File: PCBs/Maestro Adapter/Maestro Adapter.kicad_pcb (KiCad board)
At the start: 2 copper layers, 15 parts

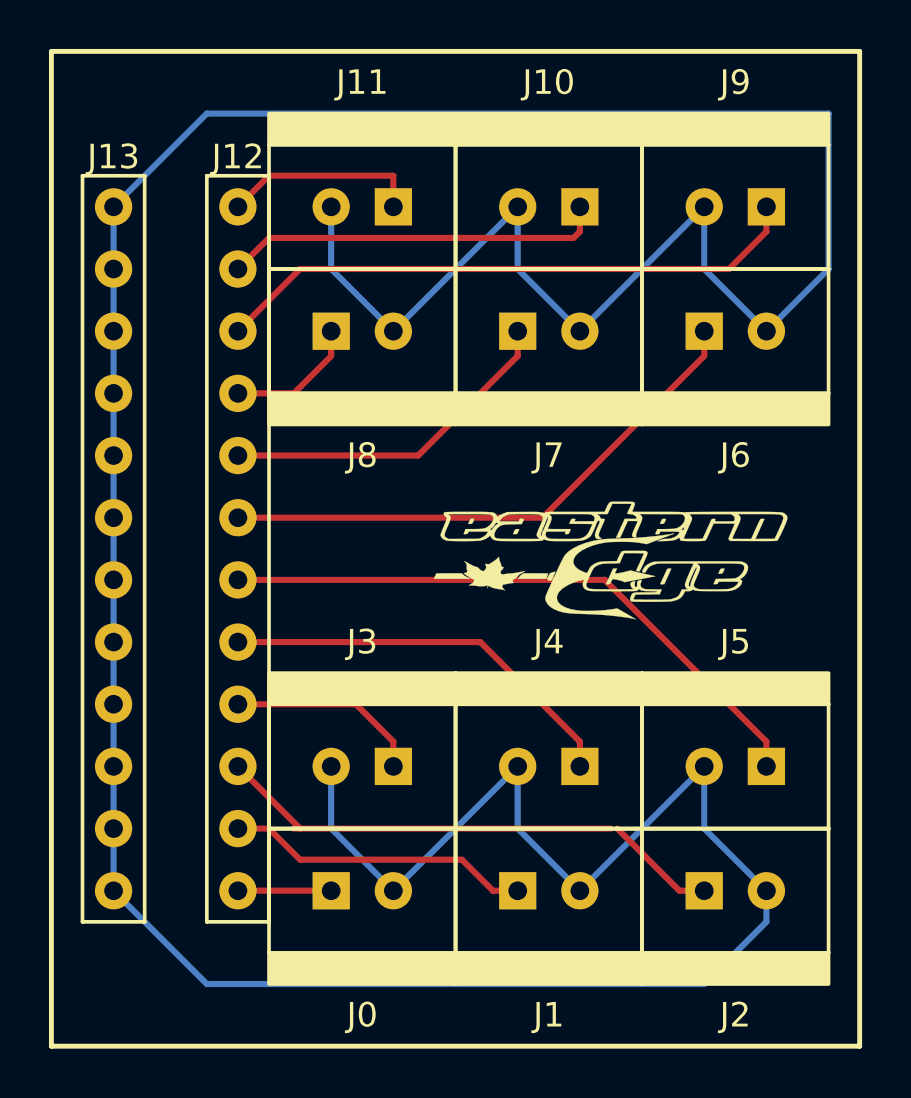
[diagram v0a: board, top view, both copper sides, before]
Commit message: added spot for missed gap in servo channels
missed a gap between channel 5 and 6. so added additional pads
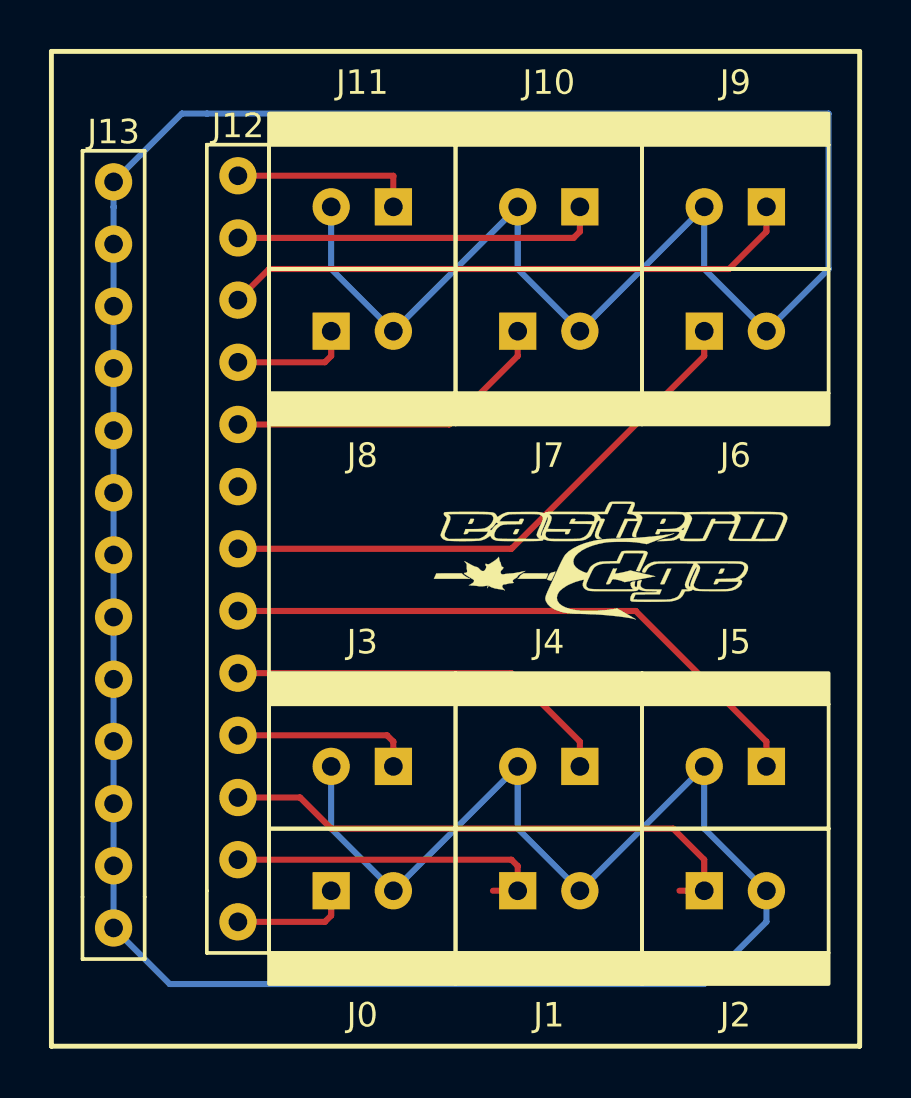
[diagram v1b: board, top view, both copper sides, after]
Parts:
- J12, J13: footprint through hole:1x12 through hole -> through hole:1x13 through hole
- moved J12 1.27 mm to (78.7, 88.9)
- moved J13 1.02 mm to (73.7, 89.2)
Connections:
- J12 pad 11: Net-(J1-Pad1) -> Net-(J12-Pad11)
- J12 pad 12: Net-(J0-Pad1) -> Net-(J1-Pad1)
- J2 pad 1: Net-(J12-Pad10) -> Net-(J12-Pad11)
- J3 pad 1: Net-(J12-Pad9) -> Net-(J12-Pad10)
- J4 pad 1: Net-(J12-Pad8) -> Net-(J12-Pad9)
- J5 pad 1: Net-(J12-Pad7) -> Net-(J12-Pad8)
- J6 pad 1: Net-(J12-Pad6) -> Net-(J12-Pad7)
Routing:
- net Net-(J12-Pad6): track 22.8 -> 0.00 mm
- net Net-(J12-Pad11): track 0.00 -> 22.4 mm
- net Net-(J12-Pad10): track 21.2 -> 7.47 mm
- net Net-(J12-Pad8): track 16.7 -> 24.8 mm
- net Net-(J12-Pad9): track 7.99 -> 16.1 mm
- net Net-(J12-Pad7): track 25.3 -> 23.3 mm
- net GND: track 164.8 -> 166.3 mm
- net Net-(J0-Pad1): track 3.81 -> 4.93 mm
- net Net-(J1-Pad1): track 12.5 -> 13.6 mm
- net Net-(J12-Pad5): track 14.1 -> 13.6 mm
- net Net-(J12-Pad3): track 24.3 -> 23.8 mm
- net Net-(J12-Pad4): track 5.45 -> 4.93 mm
- net Net-(J11-Pad1): track 8.15 -> 7.62 mm
- net Net-(J10-Pad1): track 15.6 -> 15.1 mm

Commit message: Added Colour to 3D Model
We probably have to change the footprint again anyways, but at least now its in colour!!!
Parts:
- J0, J1, J10, J11, J2, J3, J4, J5, J6, J7, J8, J9: value (none) -> Conn_01x02_Female; footprint through hole:1x2_molex_llc -> EER:1x2_molex_llc
- J12, J13: value (none) -> Conn_01x13_Male

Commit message: Completed List of suggestions
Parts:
- removed the ? at (94.0, 106.7)
- removed J0, J1, J10, J11, J2, J3, J4, J5, J6, J7, J8, J9: Conn_01x02_Female, EER:1x2_molex_llc
- added ?: , MountingHole:MountingHole_3.2mm_M3_Pad, F.Cu at (157.5, 64.8)
- added ?: , MountingHole:MountingHole_3.2mm_M3_Pad, F.Cu at (101.6, 64.8)
- added ?: , MountingHole:MountingHole_3.2mm_M3_Pad, F.Cu at (101.6, 124.5)
- added ?: , MountingHole:MountingHole_3.2mm_M3_Pad, F.Cu at (157.5, 124.5)
- added ?: , EER:EERLOGO, F.Cu at (127.0, 74.9)
- added Channel 0: , EER:1x2_molex_llc, F.Cu at (149.9, 120.7)
- added Channel 1: , EER:1x2_molex_llc, F.Cu at (149.9, 111.8)
- added Channel 10: , EER:1x2_molex_llc, F.Cu at (109.2, 77.5) (x2)
- added Channel 11: , EER:1x2_molex_llc, F.Cu at (109.2, 68.6)
- added Channel 2: , EER:1x2_molex_llc, F.Cu at (149.9, 102.9) (x3)
- added Channel 3: , EER:1x2_molex_llc, F.Cu at (149.9, 94.0)
- added Channel 4: , EER:1x2_molex_llc, F.Cu at (149.9, 85.1)
- added Channel 5: , EER:1x2_molex_llc, F.Cu at (149.9, 76.2)
- added Channel 6: , EER:1x2_molex_llc, F.Cu at (109.2, 113.0) (x2)
- added Channel 7: , EER:1x2_molex_llc, F.Cu at (109.2, 104.1)
- added Channel 8: , EER:1x2_molex_llc, F.Cu at (109.2, 95.2)
- added Channel 9: , EER:1x2_molex_llc, F.Cu at (109.2, 86.4)
- moved J13 45.1 mm to (116.8, 76.2)
- moved J12 45.0 mm to (121.9, 76.2)
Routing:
- net GND: track 166.3 -> 0.00 mm
- net Net-(J12-Pad3): track 23.8 -> 63.7 mm
- net Net-(J12-Pad4): track 4.93 -> 42.5 mm
- net Net-(J12-Pad5): track 13.6 -> 50.7 mm
- net Net-(J10-Pad1): track 15.1 -> 46.1 mm
- net Net-(J0-Pad1): track 4.93 -> 31.6 mm
- net Net-(J12-Pad10): track 7.47 -> 32.7 mm
- net Net-(J12-Pad9): track 16.1 -> 35.4 mm
- net Net-(J11-Pad1): track 7.62 -> 25.7 mm
- net Net-(J1-Pad1): track 13.6 -> 29.0 mm
- net Net-(J12-Pad8): track 24.8 -> 38.0 mm
- net Net-(J12-Pad11): track 22.4 -> 30.1 mm
- net Net-(J12-Pad7): track 23.3 -> 29.8 mm
- added copper zone on B.Cu, net GND
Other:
- board outline added: 66 x 69.8 mm
- board text added: "12 Channel Mini Maestro"

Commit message: Added another 3d model path
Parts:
- removed the Channel 10 at (109.2, 77.5) (x2)
- removed the Channel 2 at (149.9, 102.9) (x3)
- removed the Channel 6 at (109.2, 113.0) (x2)
- added Channel 10: , EER:1x2_molex_llc, F.Cu at (109.2, 77.5) (x2)
- added Channel 2: , EER:1x2_molex_llc, F.Cu at (149.9, 102.9) (x3)
- added Channel 6: , EER:1x2_molex_llc, F.Cu at (109.2, 113.0) (x2)

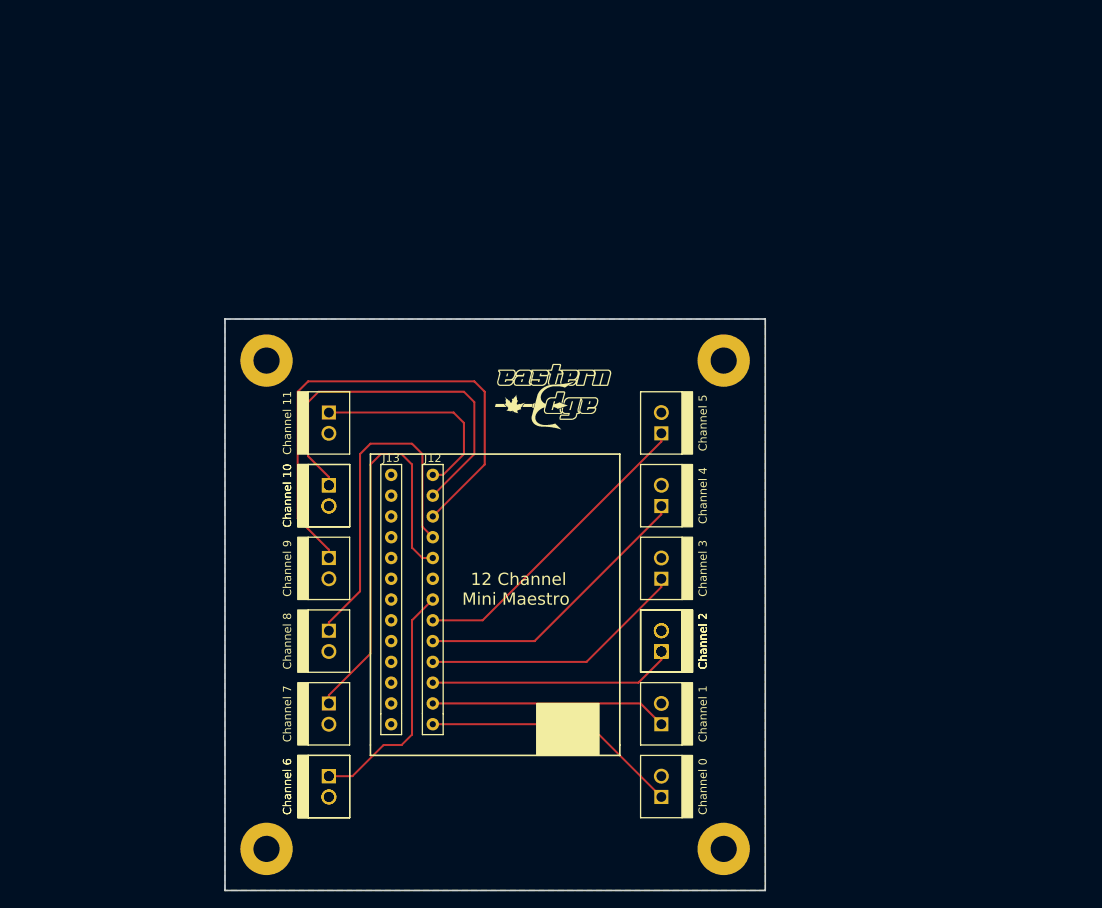
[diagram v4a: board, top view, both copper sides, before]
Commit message: Converting to 18 channel maestro
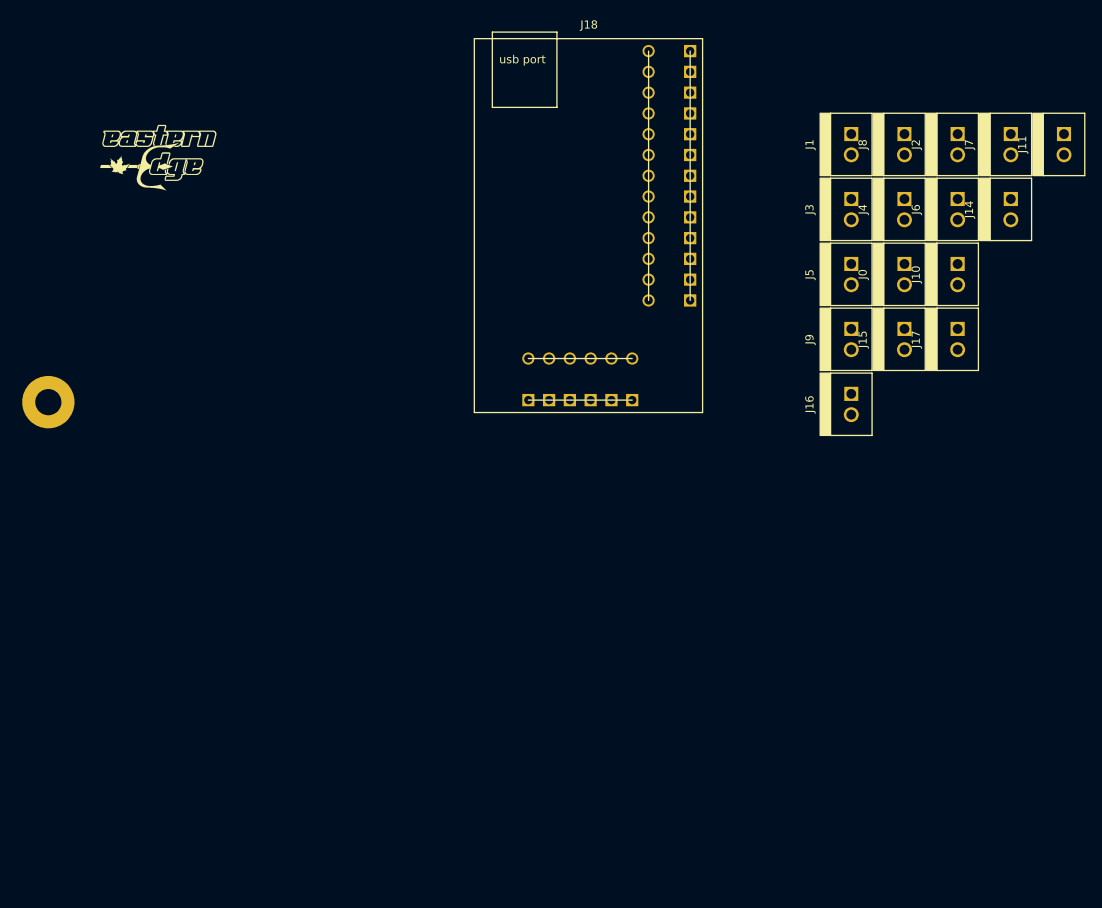
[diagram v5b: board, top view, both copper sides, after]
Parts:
- removed the ? at (157.5, 64.8)
- removed the ? at (101.6, 64.8)
- removed the ? at (101.6, 124.5)
- removed the ? at (157.5, 124.5)
- removed Channel 0: , EER:1x2_molex_llc
- removed Channel 1: , EER:1x2_molex_llc
- removed Channel 10: , EER:1x2_molex_llc (x2)
- removed Channel 11: , EER:1x2_molex_llc
- removed Channel 2: , EER:1x2_molex_llc (x3)
- removed Channel 3: , EER:1x2_molex_llc
- removed Channel 4: , EER:1x2_molex_llc
- removed Channel 5: , EER:1x2_molex_llc
- removed Channel 6: , EER:1x2_molex_llc (x2)
- removed Channel 7: , EER:1x2_molex_llc
- removed Channel 8: , EER:1x2_molex_llc
- removed Channel 9: , EER:1x2_molex_llc
- removed J12, J13: Conn_01x13_Male, through hole:1x13 through hole
- added ?: , MountingHole:MountingHole_3.2mm_M3_Pad, F.Cu at (74.9, 69.8)
- added J0: Conn_01x02_Female, EER:1x2_molex_llc, F.Cu at (179.6, 50.4)
- added J1: Conn_01x02_Female, EER:1x2_molex_llc, F.Cu at (173.1, 34.5)
- added J10: Conn_01x02_Female, EER:1x2_molex_llc, F.Cu at (186.1, 50.4)
- added J11: Conn_01x02_Female, EER:1x2_molex_llc, F.Cu at (199.1, 34.5)
- added J14: Conn_01x02_Female, EER:1x2_molex_llc, F.Cu at (192.6, 42.5)
- added J15: Conn_01x02_Female, EER:1x2_molex_llc, F.Cu at (179.6, 58.4)
- added J16: Conn_01x02_Female, EER:1x2_molex_llc, F.Cu at (173.1, 66.3)
- added J17: Conn_01x02_Female, EER:1x2_molex_llc, F.Cu at (186.1, 58.4)
- added J18: Conn_02x19_Counter_Clockwise, EER:18ChannelMaestro, F.Cu at (127.0, 71.1)
- added J2: Conn_01x02_Female, EER:1x2_molex_llc, F.Cu at (186.1, 34.5)
- added J3: Conn_01x02_Female, EER:1x2_molex_llc, F.Cu at (173.1, 42.5)
- added J4: Conn_01x02_Female, EER:1x2_molex_llc, F.Cu at (179.6, 42.5)
- added J5: Conn_01x02_Female, EER:1x2_molex_llc, F.Cu at (173.1, 50.4)
- added J6: Conn_01x02_Female, EER:1x2_molex_llc, F.Cu at (186.1, 42.5)
- added J7: Conn_01x02_Female, EER:1x2_molex_llc, F.Cu at (192.6, 34.5)
- added J8: Conn_01x02_Female, EER:1x2_molex_llc, F.Cu at (179.6, 34.5)
- added J9: Conn_01x02_Female, EER:1x2_molex_llc, F.Cu at (173.1, 58.4)
- moved ? 56.4 mm to (78.7, 45.7)
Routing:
- net Net-(J12-Pad3): track 63.7 -> 0.00 mm
- net Net-(J12-Pad5): track 50.7 -> 0.00 mm
- net Net-(J10-Pad1): track 46.1 -> 0.00 mm
- net Net-(J12-Pad4): track 42.5 -> 0.00 mm
- net Net-(J12-Pad8): track 38.0 -> 0.00 mm
- net Net-(J12-Pad9): track 35.4 -> 0.00 mm
- net Net-(J12-Pad10): track 32.7 -> 0.00 mm
- net Net-(J0-Pad1): track 31.6 -> 0.00 mm
- net Net-(J12-Pad11): track 30.1 -> 0.00 mm
- net Net-(J12-Pad7): track 29.8 -> 0.00 mm
- net Net-(J1-Pad1): track 29.0 -> 0.00 mm
- net Net-(J11-Pad1): track 25.7 -> 0.00 mm
- removed copper zone on B.Cu, net GND
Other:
- board outline removed
- board text removed: "12 Channel Mini Maestro"

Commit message: Finished pcb Layout
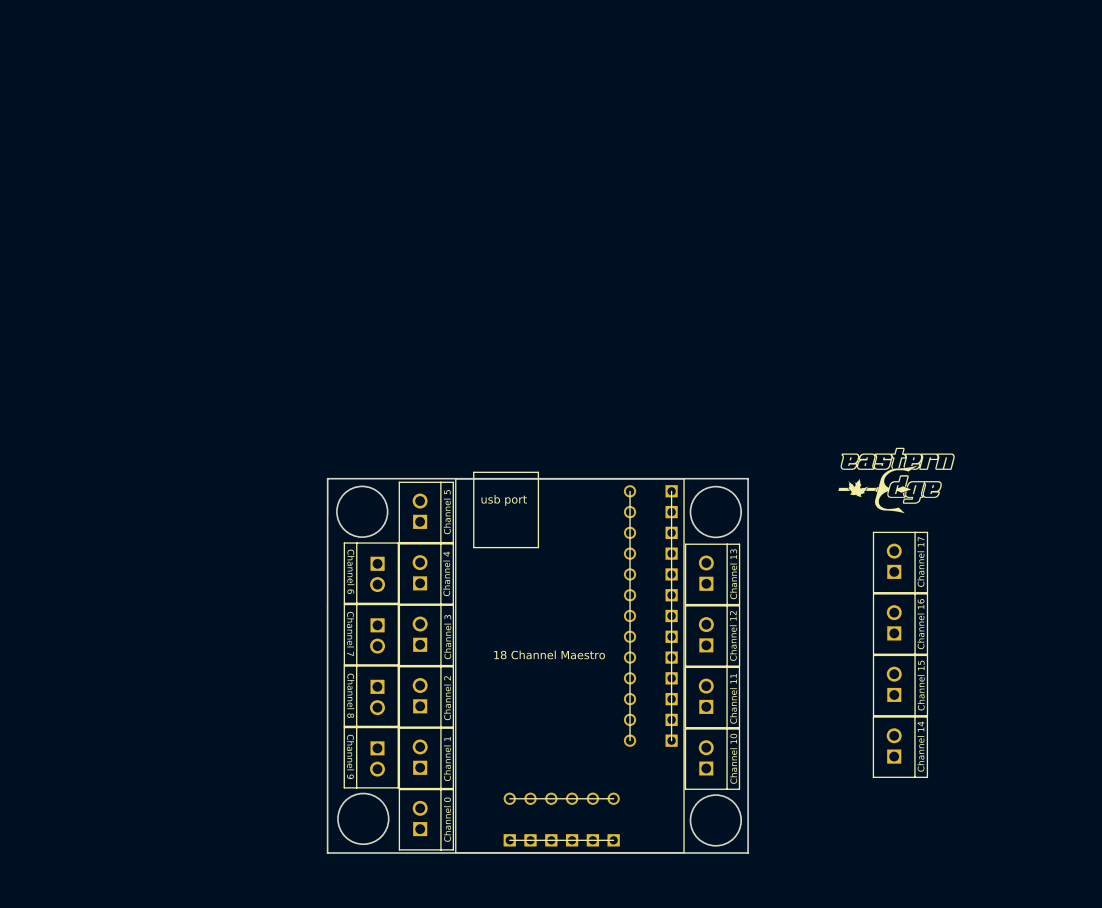
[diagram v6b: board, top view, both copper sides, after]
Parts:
- removed the ? at (74.9, 69.8)
- added Channel 12: , EER:1x2_molex_llc, F.Cu at (152.8, 102.1)
- added Channel 13: , EER:1x2_molex_llc, F.Cu at (152.8, 94.6)
- 18 Channel Maestro: renamed from J18; value Conn_02x19_Counter_Clockwise -> (none)
- Channel 0: renamed from J0; value Conn_01x02_Female -> (none)
- Channel 1: renamed from J1; value Conn_01x02_Female -> (none)
- Channel 10: renamed from J10; value Conn_01x02_Female -> (none)
- Channel 11: renamed from J11; value Conn_01x02_Female -> (none)
- Channel 14: renamed from J14; value Conn_01x02_Female -> (none)
- Channel 15: renamed from J15; value Conn_01x02_Female -> (none)
- Channel 16: renamed from J16; value Conn_01x02_Female -> (none)
- Channel 17: renamed from J17; value Conn_01x02_Female -> (none)
- Channel 2: renamed from J2; value Conn_01x02_Female -> (none)
- Channel 3: renamed from J3; value Conn_01x02_Female -> (none)
- Channel 4: renamed from J4; value Conn_01x02_Female -> (none)
- Channel 5: renamed from J5; value Conn_01x02_Female -> (none)
- Channel 6: renamed from J6; value Conn_01x02_Female -> (none)
- Channel 7: renamed from J7; value Conn_01x02_Female -> (none)
- Channel 8: renamed from J8; value Conn_01x02_Female -> (none)
- Channel 9: renamed from J9; value Conn_01x02_Female -> (none)
- moved Channel 2 101.4 mm to (117.8, 109.6)
- moved Channel 1 99.3 mm to (117.8, 117.1)
- moved ? 98.5 mm to (169.0, 85.2)
- moved Channel 0 96.5 mm to (117.8, 124.6)
- moved Channel 7 96.0 mm to (117.7, 94.6), turned to 180 degrees
- moved Channel 8 91.6 mm to (117.7, 102.1), turned to 180 degrees
- moved Channel 11 88.2 mm to (152.8, 109.6)
- moved Channel 6 81.6 mm to (117.7, 87.1), turned to 180 degrees
- moved Channel 3 81.2 mm to (117.8, 102.0)
- moved Channel 4 80.8 mm to (117.8, 94.5)
- moved Channel 9 75.5 mm to (117.7, 109.6), turned to 180 degrees
- moved Channel 14 75.1 mm to (175.8, 115.7)
- moved Channel 10 74.6 mm to (152.8, 117.2)
- moved Channel 5 66.3 mm to (117.8, 87.0)
- moved 18 Channel Maestro 53.9 mm to (124.7, 124.9)
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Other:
- board outline added: 51.4 x 45.8 mm

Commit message: Finished traces
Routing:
- net Net-(J0-Pad1): track 0.00 -> 81.6 mm
- net Net-(J1-Pad1): track 0.00 -> 77.9 mm
- net Net-(J18-Pad3): track 0.00 -> 49.3 mm
- net Net-(J13-Pad1): track 0.00 -> 45.6 mm
- net Net-(J18-Pad4): track 0.00 -> 40.3 mm
- net Net-(J18-Pad8): track 0.00 -> 35.8 mm
- net Net-(J18-Pad10): track 0.00 -> 35.2 mm
- net Net-(J18-Pad9): track 0.00 -> 34.3 mm
- net Net-(J12-Pad1): track 0.00 -> 33.6 mm
- net Net-(J18-Pad11): track 0.00 -> 33.4 mm
- net Net-(J18-Pad5): track 0.00 -> 33.2 mm
- net Net-(J18-Pad6): track 0.00 -> 29.4 mm
- net Net-(J11-Pad1): track 0.00 -> 23.5 mm
- net Net-(J10-Pad1): track 0.00 -> 11.8 mm
- added copper zone on B.Cu, net GND
